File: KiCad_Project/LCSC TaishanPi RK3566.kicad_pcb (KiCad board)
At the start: 6 copper layers, 85 x 63.4 mm, 495 parts, among them CN1 A1257WR-S-2P, CN2 GH125-S04DCA-00, CN3 GH125-S04DCA-00, J1 HDMI_A_1.4, J2 Conn_02x10_Odd_Even, Q1 CJ2301 S1, Q2 MMBT5401, Q3 MMBT5401, Q4 2SK3018, Q5 2SK3018, Q6 2SK3018, SW1 PTS815SJK250SMTRLFS, SW2 PTS815SJK250SMTRLFS, SW3 PTS815SJK250SMTRLFS, U1 SY8113BADC, U10 SY7201ABC, U11 ESD5451N, U12 ESD5451N, U13 ESD5451N, U14 ESD5451N, U15 2.4GHz, U16 ESD5451N, U17 ESD5451N, U18 ESD5451N, U2 SY8113BADC, U4 SY8089AAAC, U5 SY6280AAC, U6 SDINBDG4-8G, U7 TP5108E23E-28, U8 TP5108E23E-18, U9 SY8089AAAC, X1 XL2EL89COI-111YLC-24M, X2 32.768kHz, X3 26MHz

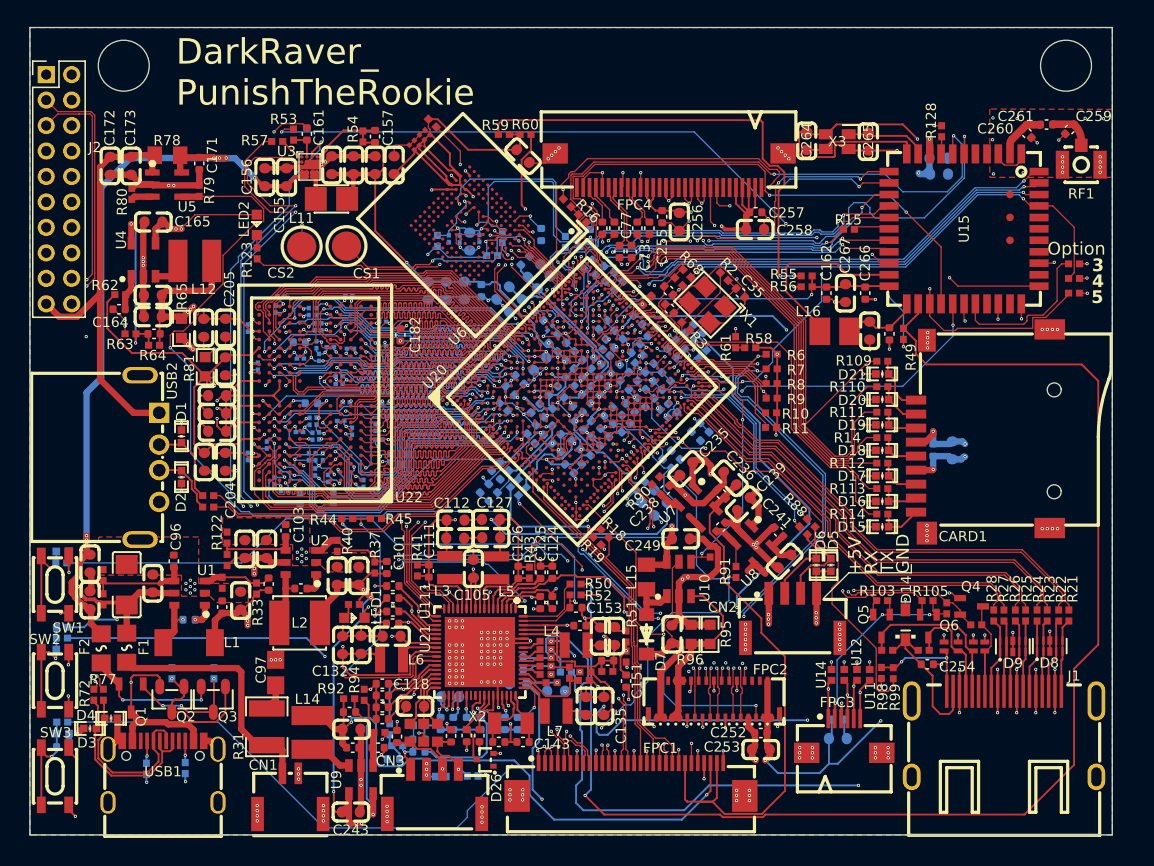
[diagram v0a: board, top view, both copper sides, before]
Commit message: Update additional PCBs
Add WIFI PCB to get best antenna
Add Display Debbugger to get interface pinout
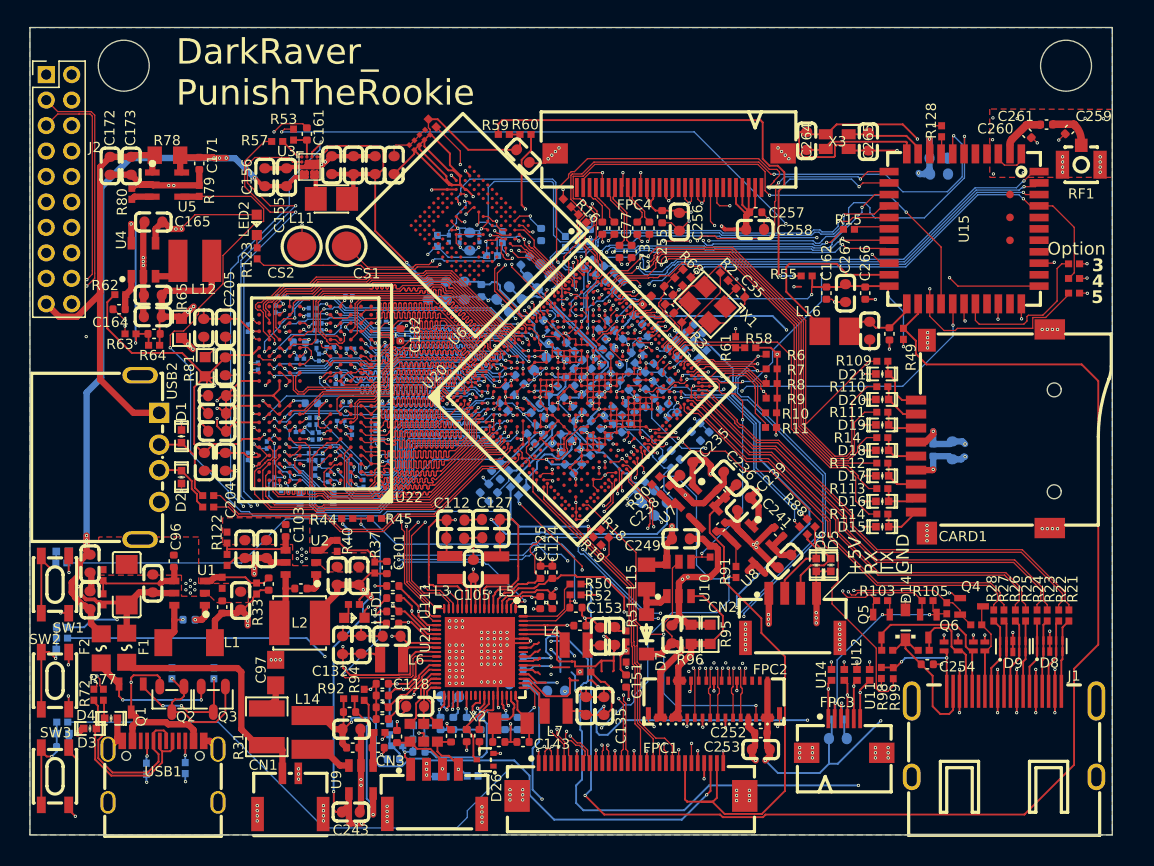
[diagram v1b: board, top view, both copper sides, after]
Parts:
- removed C111, C116, C126, C157: 1uF, Capacitor_SMD:C_0402_1005Metric
- removed R118, R124, R125, R126, R127, R38, R47, R56, R74, R76: 0Ω, LCSC Taish-easyedapro:R0402
- removed R41, R42, R43, R54: 0402WGF1000TCE, LCSC Taish-easyedapro:R0402
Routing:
- net VDD_CPU: track 54.9 -> 52.4 mm
- net VDD_LOGIC: track 51.0 -> 49.2 mm
- net VDD_GPU: track 47.1 -> 45.3 mm
- net VCCA1V8_IMAGE: track 45.7 -> 44.0 mm
